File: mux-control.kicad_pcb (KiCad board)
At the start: 2 copper layers, 14 parts, among them J1 Conn_01x08, SW1 SW_Push_Dual, SW2 SW_Push_Dual, SW3 SW_Push_Dual, SW4 SW_Push_Dual, U1 CD74HC4051E

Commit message: autorouted
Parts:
- J1: footprint Connector_PinHeader_1.00mm:PinHeader_1x08_P1.00mm_Horizontal -> Connector_PinHeader_2.00mm:PinHeader_1x08_P2.00mm_Vertical
- moved D1 26.2 mm to (153.7, 76.2), turned to 180 degrees
- moved D2 26.2 mm to (153.7, 82.5), turned to 180 degrees
- moved D3 26.2 mm to (153.7, 88.9), turned to 180 degrees
- moved D4 26.2 mm to (153.7, 95.2), turned to 180 degrees
- moved R1 24.1 mm to (160.0, 76.2)
- moved R2 24.1 mm to (160.0, 82.5)
- moved R3 24.1 mm to (160.0, 88.9)
- moved R4 24.1 mm to (160.0, 95.2)
- moved J1 18.1 mm to (139.7, 66.0), turned to 90 degrees
- moved SW3 14.2 mm to (125.7, 90.2)
- moved SW2 14.2 mm to (125.6, 77.5)
- moved SW4 14.2 mm to (125.7, 102.9)
- moved SW1 13.1 mm to (125.7, 66.0)
- moved U1 7.73 mm to (146.1, 95.2)
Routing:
- net Net-(J1-Pad1): track 0.00 -> 128.0 mm
- net Net-(SW4-Pad1): track 0.00 -> 34.6 mm
- net Net-(J1-Pad5): track 0.00 -> 32.7 mm
- net Net-(J1-Pad7): track 0.00 -> 32.2 mm
- net Net-(SW1-Pad1): track 0.00 -> 29.1 mm
- net Net-(J1-Pad4): track 0.00 -> 28.2 mm
- net Net-(J1-Pad6): track 0.00 -> 26.6 mm
- net Net-(J1-Pad2): track 0.00 -> 25.5 mm
- net Net-(J1-Pad3): track 0.00 -> 18.7 mm
- net Net-(J1-Pad8): track 0.00 -> 14.6 mm
- net Net-(SW2-Pad1): track 0.00 -> 13.9 mm
- net Net-(SW3-Pad1): track 0.00 -> 13.8 mm
- net Net-(D1-Pad2): track 0.00 -> 13.5 mm
- net Net-(D4-Pad2): track 0.00 -> 12.3 mm
- net Net-(D3-Pad2): track 0.00 -> 8.45 mm
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
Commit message: new design
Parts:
- added MO1: M1, MountingHole:MountingHole_2.1mm, F.Cu at (121.9, 62.2)
- added MO2: , MountingHole:MountingHole_2.1mm, F.Cu at (121.9, 111.8)
- added MO3: , MountingHole:MountingHole_2.1mm, F.Cu at (171.4, 62.2)
- added MO4: , MountingHole:MountingHole_2.1mm, F.Cu at (171.4, 111.8)
- D1: value LED -> LED1
- D2: value LED -> LED2
- D3: value LED -> LED3
- D4: value LED -> LED4
- moved J1 10.9 mm to (149.9, 62.2), turned to 270 degrees
- moved D4 10.5 mm to (156.2, 105.4)
- moved R4 10.5 mm to (162.6, 105.4)
- moved D1 8.03 mm to (156.2, 68.6)
- moved R1 8.03 mm to (162.6, 68.6)
- moved D3 4.58 mm to (156.2, 92.7)
- moved R3 4.58 mm to (162.6, 92.7)
- moved D2 3.59 mm to (156.2, 80.0)
- moved R2 3.59 mm to (162.6, 80.0)
- moved U1 1.27 mm to (147.3, 95.2)
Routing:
- net Net-(J1-Pad1): track 128.0 -> 0.00 mm
- net Net-(SW4-Pad1): track 34.6 -> 0.00 mm
- net Net-(J1-Pad5): track 32.7 -> 0.00 mm
- net Net-(J1-Pad7): track 32.2 -> 0.00 mm
- net Net-(SW1-Pad1): track 29.1 -> 0.00 mm
- net Net-(J1-Pad4): track 28.2 -> 0.00 mm
- net Net-(J1-Pad6): track 26.6 -> 0.00 mm
- net Net-(J1-Pad2): track 25.5 -> 0.00 mm
- net Net-(J1-Pad3): track 18.7 -> 0.00 mm
- net Net-(J1-Pad8): track 14.6 -> 0.00 mm
- net Net-(SW2-Pad1): track 13.9 -> 0.00 mm
- net Net-(SW3-Pad1): track 13.8 -> 0.00 mm
- net Net-(D1-Pad2): track 13.5 -> 0.00 mm
- net Net-(D4-Pad2): track 12.3 -> 0.00 mm
- net Net-(D3-Pad2): track 8.45 -> 0.00 mm
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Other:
- board outline added: 54.6 x 54.6 mm
- board text added: "MuxNub v1.0"

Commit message: updated freeroute tracks
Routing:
- net Net-(J1-Pad1): track 0.00 -> 152.4 mm
- net Net-(J1-Pad6): track 0.00 -> 42.6 mm
- net Net-(J1-Pad2): track 0.00 -> 41.4 mm
- net Net-(J1-Pad5): track 0.00 -> 35.3 mm
- net Net-(SW4-Pad1): track 0.00 -> 35.0 mm
- net Net-(J1-Pad7): track 0.00 -> 32.6 mm
- net Net-(J1-Pad4): track 0.00 -> 31.9 mm
- net Net-(SW1-Pad1): track 0.00 -> 29.7 mm
- net Net-(J1-Pad3): track 0.00 -> 27.5 mm
- net Net-(D4-Pad2): track 0.00 -> 23.0 mm
- net Net-(D1-Pad2): track 0.00 -> 21.7 mm
- net Net-(J1-Pad8): track 0.00 -> 20.0 mm
- net Net-(SW2-Pad1): track 0.00 -> 15.2 mm
- net Net-(SW3-Pad1): track 0.00 -> 15.0 mm
- net Net-(D3-Pad2): track 0.00 -> 12.8 mm
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
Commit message: new board tracks required
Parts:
- added G***: LOGO, muxnub:muxboy-small-reverse, F.Cu at (148.6, 86.4)
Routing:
- net Net-(J1-Pad1): track 152.4 -> 0.00 mm
- added copper zone on B.Cu, net Net-(J1-Pad1)
- added copper zone on F.Cu, net Net-(J1-Pad1)
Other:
- board text added: "MuxNub v2.0"
- board text removed: "MuxNub v1.0"

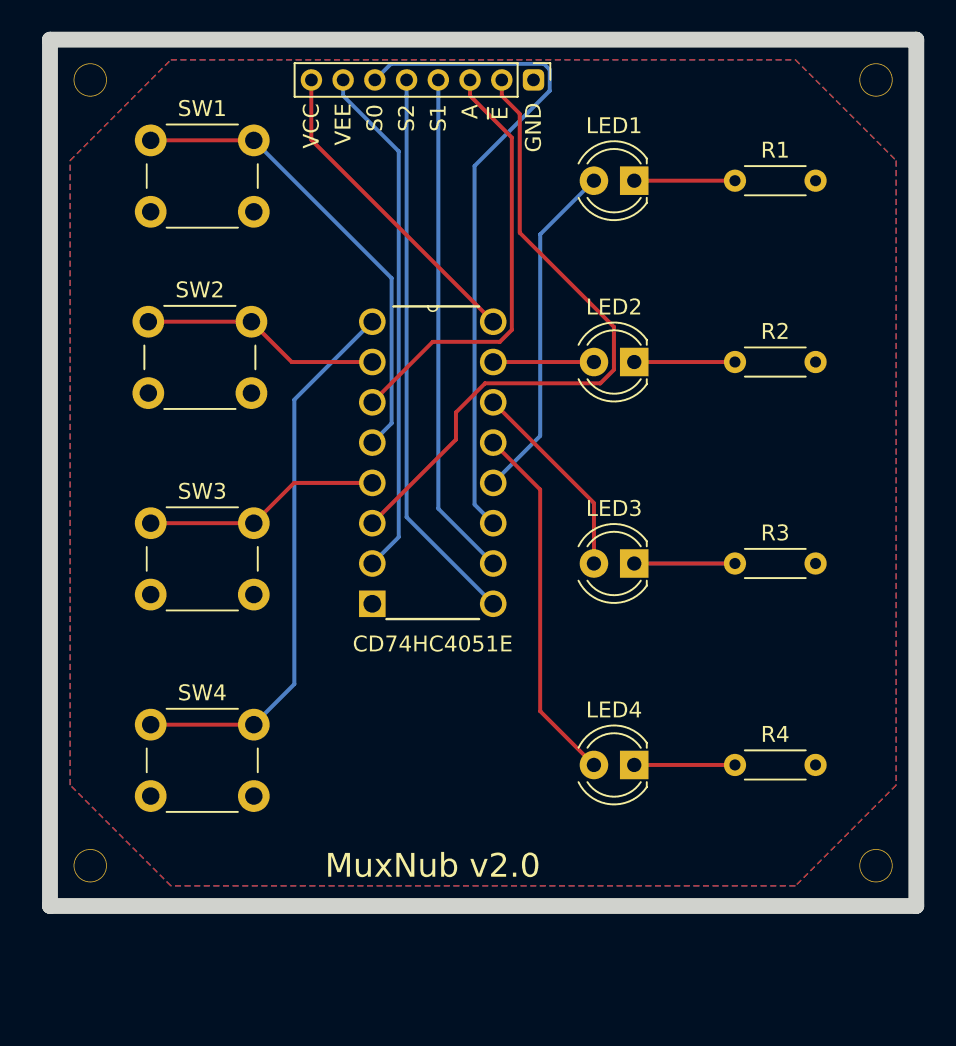
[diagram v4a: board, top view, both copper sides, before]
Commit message: kicad upgraded to nightly
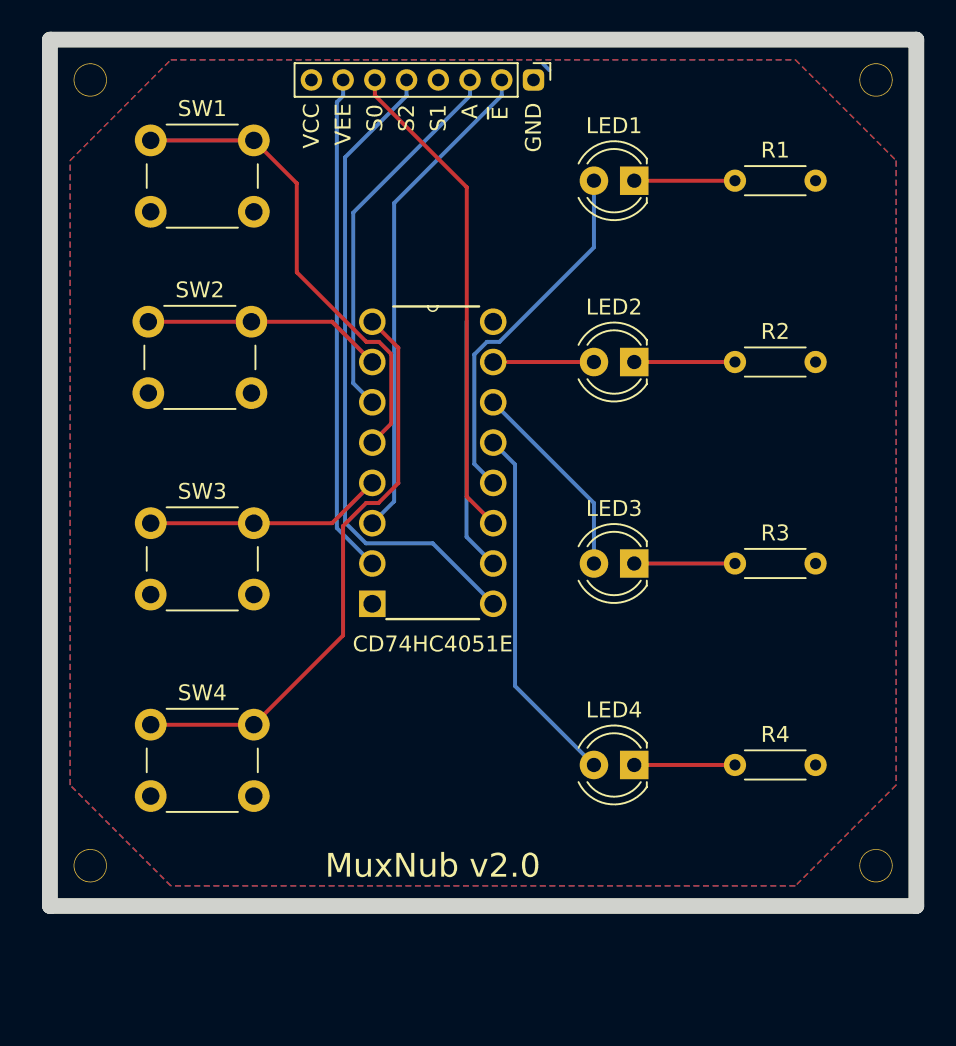
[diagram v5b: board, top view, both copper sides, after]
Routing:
- net Net-(J1-Pad8): track 20.0 -> 0.00 mm
- net Net-(J1-Pad4): track 31.9 -> 16.5 mm
- net Net-(J1-Pad6): track 42.6 -> 31.0 mm
- net Net-(J1-Pad2): track 41.4 -> 31.3 mm
- net Net-(J1-Pad5): track 35.3 -> 41.0 mm
- net Net-(J1-Pad3): track 27.5 -> 23.9 mm
- net Net-(SW4-Pad1): track 35.0 -> 36.8 mm
- net Net-(D1-Pad2): track 21.7 -> 23.1 mm
- net Net-(J1-Pad7): track 32.6 -> 31.6 mm
- added copper zone on F.Cu, net Net-(J1-Pad8)
- removed copper zone on F.Cu, net Net-(J1-Pad1)
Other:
- net class Default removed

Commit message: retracking, via to s0 required ot unlock gnd plane
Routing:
- net Net-(J1-Pad4): track 16.5 -> 41.6 mm
